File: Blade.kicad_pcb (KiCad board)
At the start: 4 copper layers, 50 x 111 mm, 118 parts, among them J1 Power, J10 2x10 Conn, J11 1x2 Conn, J12 1x3 Conn, J13 1x3 Conn, J2 ESP, J3 Conn_ARM_JTAG_SWD_10, J4 1x8 Conn, J5 1x6 Conn, J6 1x4 Conn, J7 5025700893, J8 SOIC-8 Conn, J9 1x4 Conn, Q1 SI2301CDS-T1-GE3, Q2 BSS138, Q3 BSS138, Q4 IRLML6344, Q5 MMBT3904LT1G, Q6 MMBT3904LT1G, SW1 BSI-10, SW2 BOOT, SW3 EN, SW4 UP, SW5 DOWN, SW6 SEL, SW7 BACK, U1 ESP32-S3-WROOM-1-N16, U2 CH340C, U3 AMS1117, U4 AP2112K-1.8, U5 TXS0108EPW, U6 W25Q128, U7 AT24C256C, U8 INA219AxD, U9 TSOP382xx

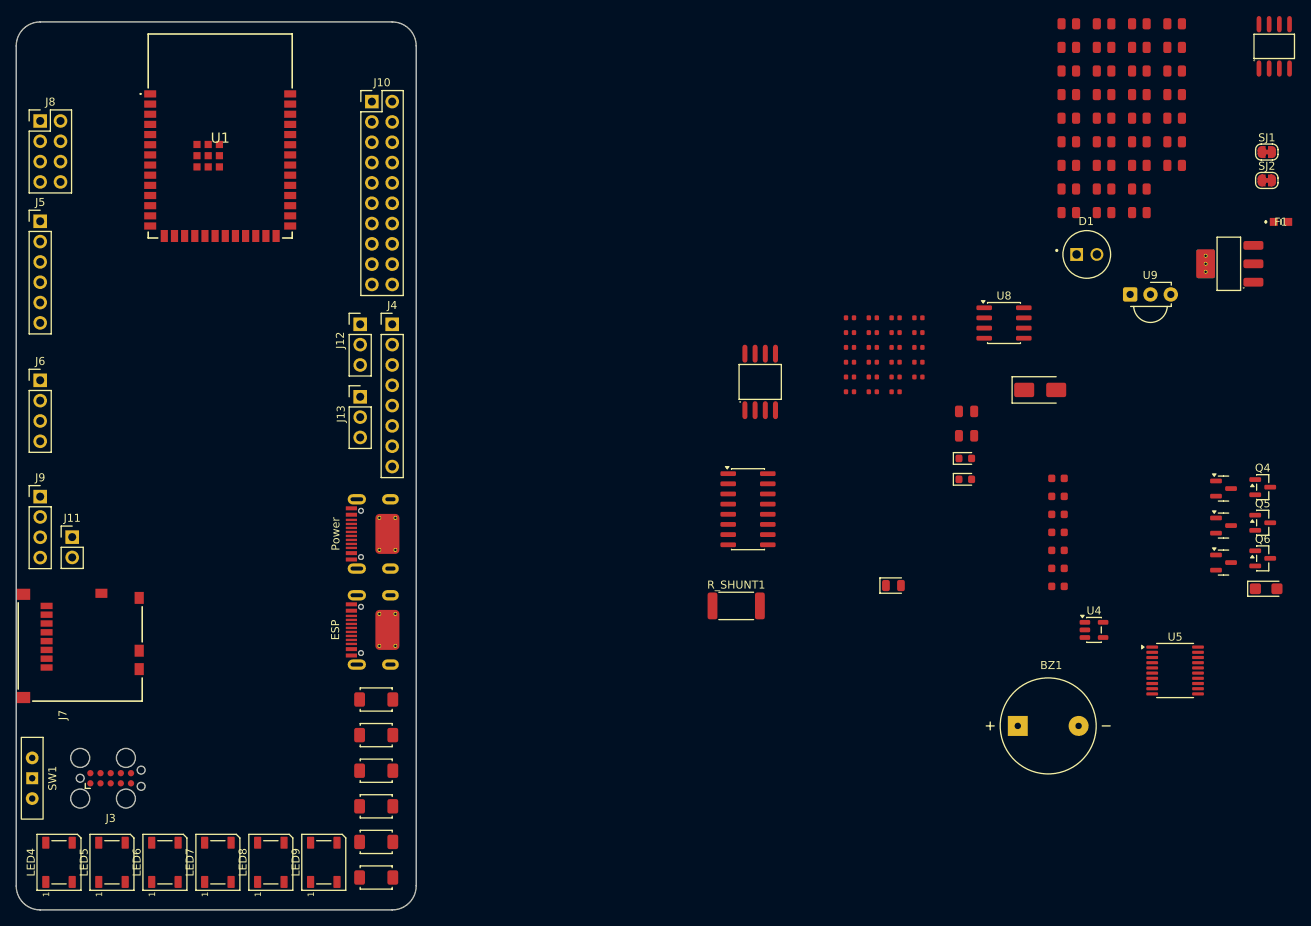
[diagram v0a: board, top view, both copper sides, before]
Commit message: Add Blade image and update README with board section
- Added Blade.png image to the repository.
- Updated README.md to include a new section for the board with the Blade image.
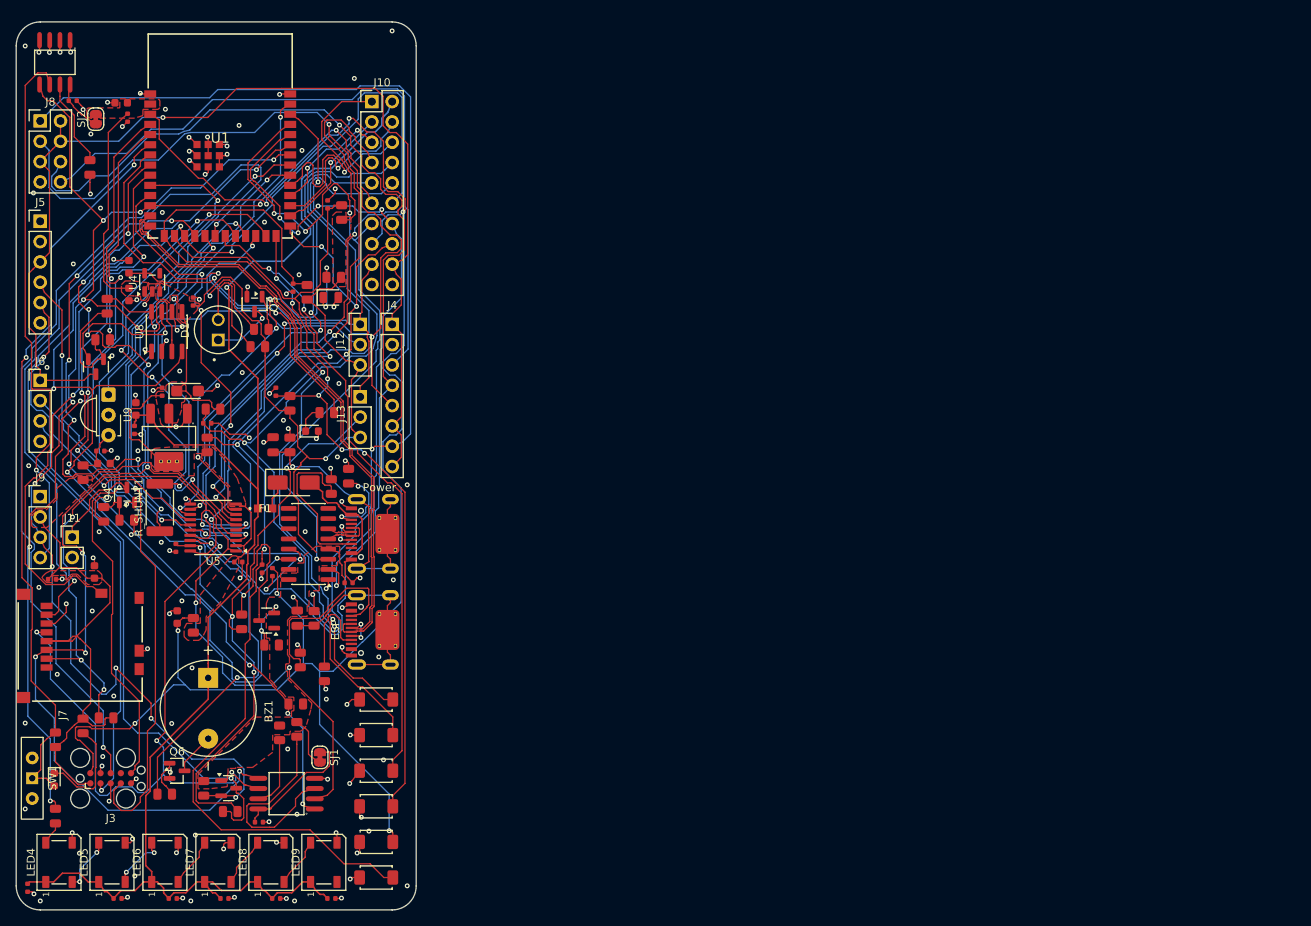
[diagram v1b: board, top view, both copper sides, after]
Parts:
- moved R32 160.0 mm to (110.9, 139.7), turned to 90 degrees
- moved R19 158.5 mm to (114.4, 138.0), turned to 90 degrees
- moved R25 158.0 mm to (110.9, 149.3), turned to -90 degrees
- moved R31 153.6 mm to (124.6, 146.5)
- moved U7 152.4 mm to (110.8, 55.1), turned to 180 degrees
- moved R10 147.1 mm to (132.8, 148.7), turned to 180 degrees
- moved SJ2 146.6 mm to (115.9, 62.1), turned to 90 degrees
- moved R16 142.6 mm to (117.2, 137.0)
- moved Q4 142.0 mm to (119.8, 109.1), turned to 90 degrees
- moved Q1 141.8 mm to (116.0, 93.1), turned to -90 degrees
- moved SJ1 140.5 mm to (144.0, 141.9), turned to -90 degrees
- moved R24 138.4 mm to (114.4, 106.3), turned to -90 degrees
- moved Q6 138.3 mm to (126.1, 143.6)
- moved C2 137.1 mm to (127.4, 96.1)
- moved U3 134.4 mm to (125.1, 101.9), turned to 90 degrees
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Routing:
- net +3.3V: track 0.00 -> 262.2 mm, vias 0 -> 1
- net /I2C_SCL: track 0.00 -> 234.2 mm, vias 0 -> 7
- net /ESP_EN: track 0.00 -> 217.7 mm, vias 0 -> 7
- net /VCC_5V: track 0.00 -> 191.6 mm, vias 0 -> 1
- net /I2C_SDA: track 0.00 -> 189.2 mm, vias 0 -> 11
- net /SPI_SCLK: track 0.00 -> 182.1 mm, vias 0 -> 10
- net /SPI_MISO: track 0.00 -> 152.6 mm, vias 0 -> 8
- net /HSPI_CS: track 0.00 -> 148.4 mm, vias 0 -> 2
- net /HSPI_SCLK: track 0.00 -> 143.1 mm, vias 0 -> 2
- net /HSPI_MOSI: track 0.00 -> 140.4 mm, vias 0 -> 3
- net /VCC_TGT: track 0.00 -> 138.3 mm, vias 0 -> 1
- net /SPI_MOSI: track 0.00 -> 133.9 mm, vias 0 -> 8
- net /HSPI_MISO: track 0.00 -> 133.4 mm, vias 0 -> 3
- net /BTN_BOOT: track 0.00 -> 132.9 mm, vias 0 -> 5
- net GND: track 0.00 -> 126.7 mm, vias 0 -> 135
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- added copper zone on F.Cu, net +3.3V
- added copper zone on In2.Cu, net GND
- removed copper zone on In2.Cu, net +3.3V
